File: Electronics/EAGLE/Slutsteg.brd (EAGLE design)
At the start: 100 x 160 mm, 150 parts, among them CN1 OSTYK33102030-2, CN2 OSTYK33102030-2, CN3 OSTYK33102030-2, CN4 OSTYK33102030-2, IC1 SPX1117M3-L-3-3_TR, IC10 LM324D, IC11 L78M12ABDT-TR, IC3 ESP32-WROVER-IE-4MB, IC4 TM8211, IC6 TPA3244DDWR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

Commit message: Changed components
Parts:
- C18: value ECA-1HM471B -> 16PK470MEFC8X11.5; device SamacSys_Parts:CAPPRD500W65D1000H2200 -> SamacSys_Parts:CAPPRD350W60D825H1300
- C30, C31: device SamacSys_Parts:CAPPRD500W65D1000H2200 -> SamacSys_Parts:CAPPRD500W60D1300H2650
- C47: device TPA3244.dbl:SAMACSYS_PARTS_CAPPRD500W65D1000H2200 -> SamacSys_Parts:CAPPRD350W60D825H1300
- C63, C64: device TPA3244.dbl:SAMACSYS_PARTS_CAPPRD500W65D1000H2200 -> SamacSys_Parts:CAPPRD500W60D1300H2650
- L1, L2, L3, L4: value 74477010 -> 48100SC; device SamacSys_Parts:WE-PD_1260/1245/1280/121054 -> SamacSys_Parts:INDPM122122X600N
- moved IC10 303.9 mm to (55.0, 153.0), turned to 90 degrees
- moved J1 27.0 mm to (95.0, 125.4)
- moved IC3 10.0 mm to (82.8, 144.9)
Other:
- outline, holes or cut-outs redrawn

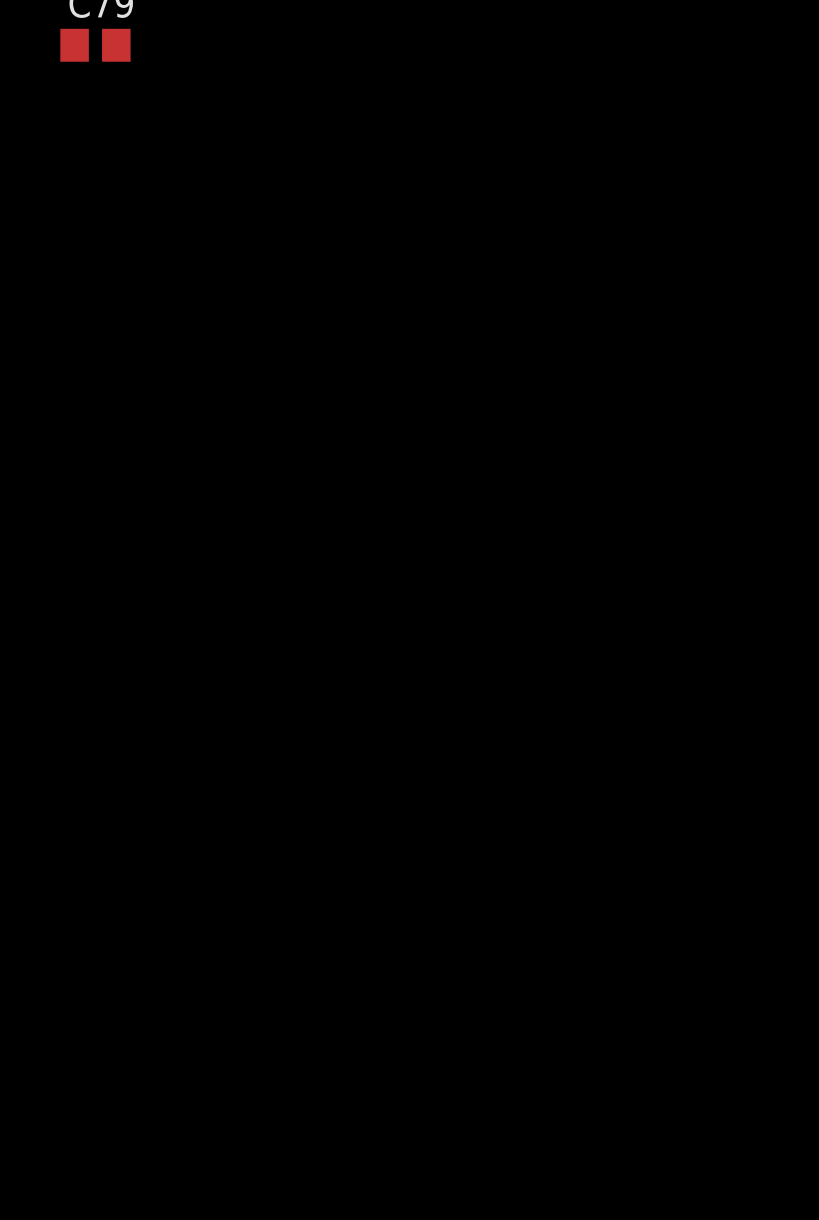
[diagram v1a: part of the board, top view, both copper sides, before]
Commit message: Lagt till 3.5mm input och vridpot för Basen
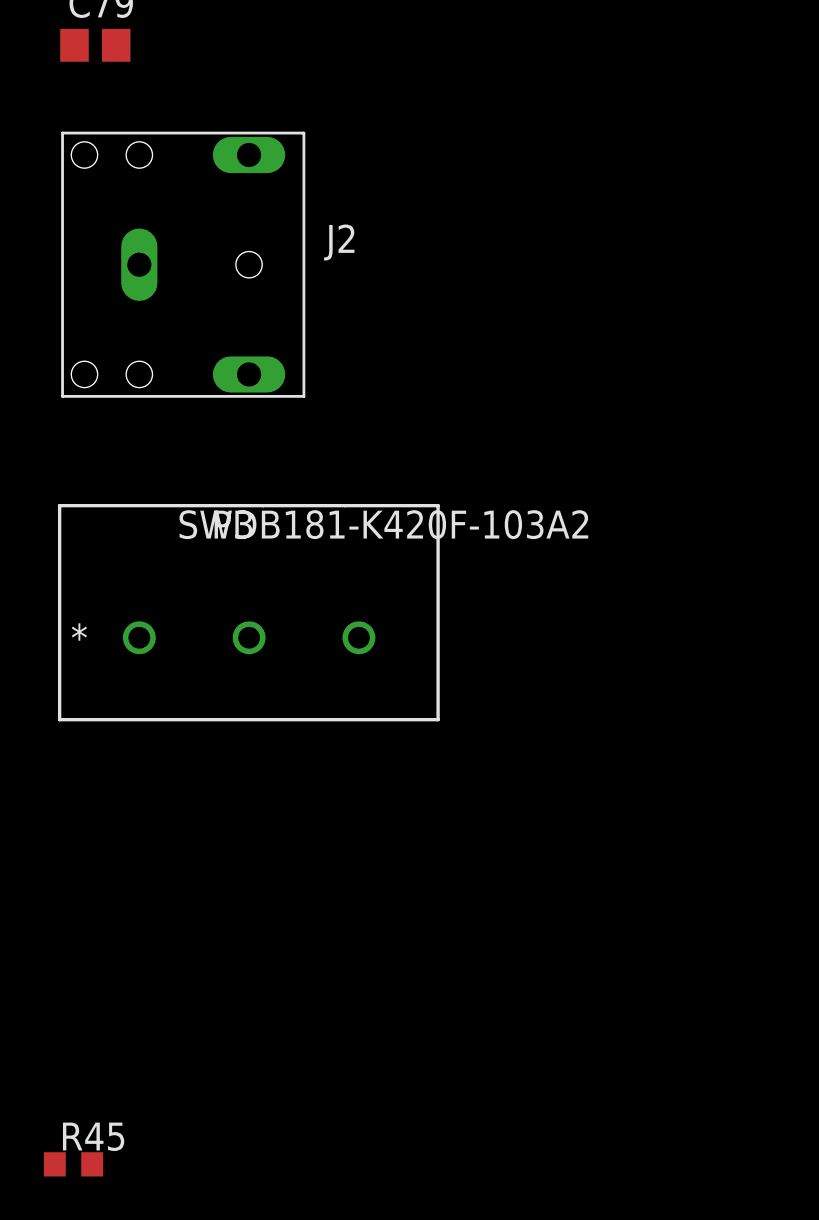
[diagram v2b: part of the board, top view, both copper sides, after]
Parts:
- added J2: JW-PJ-307-4H, jack_04:JW-PJ-307-4H
- added R45: 10K/5%/0.1W, rcl:R0603
- added SW3: PDB181-K420F-103A2, PDB181-K420F-103A2:SW_420F-103A2_BRN
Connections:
- new net N$4: IC10.13, R45.2, SW3.1
- net 6V_BUFFER: now also IC10.12
- net BASE_OUT: now also IC10.14, SW3.2, SW3.3; no longer C75.1, R33.1
- net BASE_VOLUME: now also C75.1, R33.1, R45.1
- net GND: now also J2.1
- net SIG_IN_LEFT: now also J2.5
- net SIG_IN_RIGHT: now also J2.2

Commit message: FIxat lite kondensatorer
:)
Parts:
- C27, C28, C29, C32, C55, C58, C61, C62, C75: value 33nF/25V -> 33nF/50V
- C71, C72, C74, C77, C80, C81: value 100nF/25V -> 100nF/50V
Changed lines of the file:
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@@
 <attribute name="VALUE" x="114.635" y="127.965" size="1.27" layer="27"/>
 </element>
-<element name="C62" library="rcl" library_urn="urn:adsk.eagle:library:334" package="C0603" package3d_urn="urn:adsk.eagle:package:23616/2" value="33nF/25V" x="115.27" y="124.79" smashed="yes">
+<element name="C62" library="rcl" library_urn="urn:adsk.eagle:library:334" package="C0603" package3d_urn="urn:adsk.eagle:package:23616/2" value="33nF/50V" x="115.27" y="124.79" smashed="yes">
 <attribute name="NAME" x="114.635" y="125.425" size="1.27" layer="25"/>
 <attribute name="POPULARITY" value="73" x="115.27" y="124.79" size="1.778" layer="27" display="off"/>
@@
 <attribute name="VALUE" x="114.635" y="122.885" size="1.27" layer="27"/>
 </element>
-<element name="C58" library="rcl" library_urn="urn:adsk.eagle:library:334" package="C0603" package3d_urn="urn:adsk.eagle:package:23616/2" value="33nF/25V" x="115.27" y="119.71" smashed="yes">
+<element name="C58" library="rcl" library_urn="urn:adsk.eagle:library:334" package="C0603" package3d_urn="urn:adsk.eagle:package:23616/2" value="33nF/50V" x="115.27" y="119.71" smashed="yes">
 <attribute name="NAME" x="114.635" y="120.345" size="1.27" layer="25"/>
 <attribute name="POPULARITY" value="73" x="115.27" y="119.71" size="1.778" layer="27" display="off"/>
@@
 <attribute name="VALUE" x="114.635" y="117.805" size="1.27" layer="27"/>
 </element>
-<element name="C55" library="rcl" library_urn="urn:adsk.eagle:library:334" package="C0603" package3d_urn="urn:adsk.eagle:package:23616/2" value="33nF/25V" x="115.27" y="114.63" smashed="yes">
+<element name="C55" library="rcl" library_urn="urn:adsk.eagle:library:334" package="C0603" package3d_urn="urn:adsk.eagle:package:23616/2" value="33nF/50V" x="115.27" y="114.63" smashed="yes">
 <attribute name="NAME" x="114.635" y="115.265" size="1.27" layer="25"/>
 <attribute name="POPULARITY" value="73" x="115.27" y="114.63" size="1.778" layer="27" display="off"/>
@@
 <attribute name="VALUE" x="114.635" y="112.725" size="1.27" layer="27"/>
 </element>
-<element name="C61" library="rcl" library_urn="urn:adsk.eagle:library:334" package="C0603" package3d_urn="urn:adsk.eagle:package:23616/2" value="33nF/25V" x="115.27" y="109.55" smashed="yes">
+<element name="C61" library="rcl" library_urn="urn:adsk.eagle:library:334" package="C0603" package3d_urn="urn:adsk.eagle:package:23616/2" value="33nF/50V" x="115.27" y="109.55" smashed="yes">
 <attribute name="NAME" x="114.635" y="110.185" size="1.27" layer="25"/>
 <attribute name="POPULARITY" value="73" x="115.27" y="109.55" size="1.778" layer="27" display="off"/>
@@
 <attribute name="VALUE" x="43.65" y="98" size="1.27" layer="27" align="center"/>
 </element>
-<element name="C27" library="rcl" library_urn="urn:adsk.eagle:library:334" package="C0603" package3d_urn="urn:adsk.eagle:package:23616/2" value="33nF/25V" x="-45.32" y="239.88" smashed="yes">
+<element name="C27" library="rcl" library_urn="urn:adsk.eagle:library:334" package="C0603" package3d_urn="urn:adsk.eagle:package:23616/2" value="33nF/50V" x="-45.32" y="239.88" smashed="yes">
 <attribute name="NAME" x="-45.955" y="240.515" size="1.27" layer="25"/>
 <attribute name="POPULARITY" value="73" x="-45.32" y="239.88" size="1.778" layer="27" display="off"/>
@@
 <attribute name="VALUE" x="-45.955" y="237.975" size="1.27" layer="27"/>
 </element>
-<element name="C29" library="rcl" library_urn="urn:adsk.eagle:library:334" package="C0603" package3d_urn="urn:adsk.eagle:package:23616/2" value="33nF/25V" x="-45.32" y="234.8" smashed="yes">
+<element name="C29" library="rcl" library_urn="urn:adsk.eagle:library:334" package="C0603" package3d_urn="urn:adsk.eagle:package:23616/2" value="33nF/50V" x="-45.32" y="234.8" smashed="yes">
 <attribute name="NAME" x="-45.955" y="235.435" size="1.27" layer="25"/>
 <attribute name="POPULARITY" value="73" x="-45.32" y="234.8" size="1.778" layer="27" display="off"/>
@@
 <attribute name="VALUE" x="70.965" y="105.705" size="1.27" layer="27" rot="R270"/>
 </element>
-<element name="C32" library="rcl" library_urn="urn:adsk.eagle:library:334" package="C0603" package3d_urn="urn:adsk.eagle:package:23616/2" value="33nF/25V" x="35.68" y="76.44" smashed="yes">
+<element name="C32" library="rcl" library_urn="urn:adsk.eagle:library:334" package="C0603" package3d_urn="urn:adsk.eagle:package:23616/2" value="33nF/50V" x="35.68" y="76.44" smashed="yes">
 <attribute name="NAME" x="35.045" y="77.075" size="1.27" layer="25"/>
 <attribute name="POPULARITY" value="73" x="35.68" y="76.44" size="1.778" layer="27" display="off"/>
@@
 <attribute name="VALUE" x="35.045" y="74.535" size="1.27" layer="27"/>
 </element>
-<element name="C28" library="rcl" library_urn="urn:adsk.eagle:library:334" package="C0603" package3d_urn="urn:adsk.eagle:package:23616/2" value="33nF/25V" x="35.68" y="79.36" smashed="yes">
+<element name="C28" library="rcl" library_urn="urn:adsk.eagle:library:334" package="C0603" package3d_urn="urn:adsk.eagle:package:23616/2" value="33nF/50V" x="35.68" y="79.36" smashed="yes">
 <attribute name="NAME" x="35.045" y="79.995" size="1.27" layer="25"/>
 <attribute name="POPULARITY" value="73" x="35.68" y="79.36" size="1.778" layer="27" display="off"/>
@@
 <attribute name="VALUE" x="-157.245" y="204.905" size="1.27" layer="27"/>
 </element>
-<element name="C75" library="rcl" library_urn="urn:adsk.eagle:library:334" package="C0603" package3d_urn="urn:adsk.eagle:package:23616/2" value="33nF/25V" x="-156.61" y="203" smashed="yes">
+<element name="C75" library="rcl" library_urn="urn:adsk.eagle:library:334" package="C0603" package3d_urn="urn:adsk.eagle:package:23616/2" value="33nF/50V" x="-156.61" y="203" smashed="yes">
 <attribute name="NAME" x="-157.245" y="203.635" size="1.27" layer="25"/>
 <attribute name="POPULARITY" value="73" x="-156.61" y="203" size="1.778" layer="27" display="off"/>
@@
 <attribute name="VALUE" x="-164.23" y="206.81" size="1.27" layer="27" align="center"/>
 </element>
-<element name="C71" library="rcl" library_urn="urn:adsk.eagle:library:334" package="C0603" package3d_urn="urn:adsk.eagle:package:23616/2" value="100nF/25V" x="-165.5" y="199.19" smashed="yes">
+<element name="C71" library="rcl" library_urn="urn:adsk.eagle:library:334" package="C0603" package3d_urn="urn:adsk.eagle:package:23616/2" value="100nF/50V" x="-165.5" y="199.19" smashed="yes">
 <attribute name="NAME" x="-166.135" y="199.825" size="1.27" layer="25"/>
 <attribute name="POPULARITY" value="73" x="-165.5" y="199.19" size="1.778" layer="27" display="off"/>
@@
 <attribute name="VALUE" x="-166.135" y="197.285" size="1.27" layer="27"/>
 </element>
-<element name="C72" library="rcl" library_urn="urn:adsk.eagle:library:334" package="C0603" package3d_urn="urn:adsk.eagle:package:23616/2" value="100nF/25V" x="-165.5" y="195.38" smashed="yes">
+<element name="C72" library="rcl" library_urn="urn:adsk.eagle:library:334" package="C0603" package3d_urn="urn:adsk.eagle:package:23616/2" value="100nF/50V" x="-165.5" y="195.38" smashed="yes">
 <attribute name="NAME" x="-166.135" y="196.015" size="1.27" layer="25"/>
 <attribute name="POPULARITY" value="73" x="-165.5" y="195.38" size="1.778" layer="27" display="off"/>
@@
 <attribute name="VALUE" x="-166.135" y="182.045" size="1.27" layer="27"/>
 </element>
-<element name="C81" library="rcl" library_urn="urn:adsk.eagle:library:334" package="C0603" package3d_urn="urn:adsk.eagle:package:23616/2" value="100nF/25V" x="-165.5" y="180.14" smashed="yes">
+<element name="C81" library="rcl" library_urn="urn:adsk.eagle:library:334" package="C0603" package3d_urn="urn:adsk.eagle:package:23616/2" value="100nF/50V" x="-165.5" y="180.14" smashed="yes">
 <attribute name="NAME" x="-166.135" y="180.775" size="1.27" layer="25"/>
 <attribute name="POPULARITY" value="73" x="-165.5" y="180.14" size="1.778" layer="27" display="off"/>
@@
 <attribute name="VALUE" x="-166.135" y="178.235" size="1.27" layer="27"/>
 </element>
-<element name="C80" library="rcl" library_urn="urn:adsk.eagle:library:334" package="C0603" package3d_urn="urn:adsk.eagle:package:23616/2" value="100nF/25V" x="-165.5" y="176.33" smashed="yes">
+<element name="C80" library="rcl" library_urn="urn:adsk.eagle:library:334" package="C0603" package3d_urn="urn:adsk.eagle:package:23616/2" value="100nF/50V" x="-165.5" y="176.33" smashed="yes">
 <attribute name="NAME" x="-166.135" y="176.965" size="1.27" layer="25"/>
 <attribute name="POPULARITY" value="73" x="-165.5" y="176.33" size="1.778" layer="27" display="off"/>
@@
 <attribute name="VENDOR" value="Bourns Electronics" x="-182.01" y="185.22" size="1.778" layer="27" display="off"/>
 </element>
-<element name="C77" library="rcl" library_urn="urn:adsk.eagle:library:334" package="C0603" package3d_urn="urn:adsk.eagle:package:23616/2" value="100nF/25V" x="-165.5" y="129.34" smashed="yes">
+<element name="C77" library="rcl" library_urn="urn:adsk.eagle:library:334" package="C0603" package3d_urn="urn:adsk.eagle:package:23616/2" value="100nF/50V" x="-165.5" y="129.34" smashed="yes">
 <attribute name="NAME" x="-166.135" y="129.975" size="1.27" layer="25"/>
 <attribute name="POPULARITY" value="73" x="-165.5" y="129.34" size="1.778" layer="27" display="off"/>
@@
 <attribute name="VALUE" x="-166.135" y="127.435" size="1.27" layer="27"/>
 </element>
-<element name="C74" library="rcl" library_urn="urn:adsk.eagle:library:334" package="C0603" package3d_urn="urn:adsk.eagle:package:23616/2" value="100nF/25V" x="-165.5" y="124.26" smashed="yes">
+<element name="C74" library="rcl" library_urn="urn:adsk.eagle:library:334" package="C0603" package3d_urn="urn:adsk.eagle:package:23616/2" value="100nF/50V" x="-165.5" y="124.26" smashed="yes">
 <attribute name="NAME" x="-166.135" y="124.895" size="1.27" layer="25"/>
 <attribute name="POPULARITY" value="73" x="-165.5" y="124.26" size="1.778" layer="27" display="off"/>

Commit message: Fixa en sista kondensator
:DDDDDDD
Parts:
- C73: value 150nF/25V -> 150nF/50V
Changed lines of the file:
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@@
 <attribute name="VALUE" x="-139.465" y="289.995" size="1.27" layer="27"/>
 </element>
-<element name="C73" library="rcl" library_urn="urn:adsk.eagle:library:334" package="C0603" package3d_urn="urn:adsk.eagle:package:23616/2" value="150nF/25V" x="-138.83" y="288.09" smashed="yes">
+<element name="C73" library="rcl" library_urn="urn:adsk.eagle:library:334" package="C0603" package3d_urn="urn:adsk.eagle:package:23616/2" value="150nF/50V" x="-138.83" y="288.09" smashed="yes">
 <attribute name="NAME" x="-139.465" y="288.725" size="1.27" layer="25"/>
 <attribute name="POPULARITY" value="73" x="-138.83" y="288.09" size="1.778" layer="27" display="off"/>

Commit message: Snyggat till kopplingar
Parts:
- removed CN4: OSTYK33102030-2, OSTYK33108030:OSTYK33108030-2
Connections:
- net SPEAKER_B_0: now also CN3.2
- net SPEAKER_B_1: now also CN3.1
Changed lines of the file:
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@@
 <attribute name="NAME" x="87" y="43.13" size="1.27" layer="25" rot="R270"/>
-</element>
-<element name="CN4" library="OSTYK33108030" package="OSTYK33108030-2" override_package3d_urn="urn:adsk.eagle:package:27162207/2" override_package_urn="urn:adsk.eagle:footprint:27162209/1" value="OSTYK33102030-2" x="95" y="14" smashed="yes" rot="R270">
-<attribute name="NAME" x="87" y="13.13" size="1.27" layer="25" rot="R270"/>
 </element>
 <element name="IC11" library="SamacSys_Parts" package="TO228P972X240-3N" value="L78M12ABDT-TR" x="-202" y="-15" smashed="yes">
@@
 <contactref element="C69" pad="1"/>
 <contactref element="C67" pad="1"/>
+<contactref element="CN3" pad="2"/>
 <wire x1="114.42" y1="140.03" x2="114.42" y2="129.87" width="0" layer="19" extent="1-1"/>
 <wire x1="148.16" y1="167.97" x2="114.42" y2="140.03" width="0" layer="19" extent="1-1"/>
 <wire x1="181.18" y1="198.45" x2="148.16" y2="167.97" width="0" layer="19" extent="1-1"/>
 <wire x1="181.07" y1="213.69" x2="181.18" y2="198.45" width="0" layer="19" extent="1-1"/>
+<wire x1="95" y1="35.75" x2="114.42" y2="129.87" width="0" layer="19" extent="1-1"/>
 </signal>
 <signal name="N$2">
@@
 <contactref element="C70" pad="2"/>
 <contactref element="C68" pad="2"/>
+<contactref element="CN3" pad="1"/>
 <wire x1="116.12" y1="155.27" x2="116.12" y2="134.95" width="0" layer="19" extent="1-1"/>
 <wire x1="130.38" y1="167.97" x2="116.12" y2="155.27" width="0" layer="19" extent="1-1"/>
 <wire x1="163.4" y1="198.45" x2="130.38" y2="167.97" width="0" layer="19" extent="1-1"/>
 <wire x1="145.75" y1="213.69" x2="163.4" y2="198.45" width="0" layer="19" extent="1-1"/>
+<wire x1="95" y1="44" x2="116.12" y2="134.95" width="0" layer="19" extent="1-1"/>
 </signal>
 <signal name="N$37">
